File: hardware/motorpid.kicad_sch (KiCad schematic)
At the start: 108 parts, among them J1 BNC, J2 BNC, J3 BNC, J4 MOTOR + - shield, J5 POT 1 (+) 2 (wiper) 3 (-), J6 +15 / GND / -15, M1 fader motor, Q1 MJD44H11, Q2 MJD45H11, SW1 TARGET SOURCE, SW2 LOOP, SW3 D IN / OFF, SW4 I IN / OFF, SW5 D CAPACITOR, U1 LM321, U2 LM321, U3 LM321, U4 LM321, U5 LM321, U6 LM321, U7 LM321

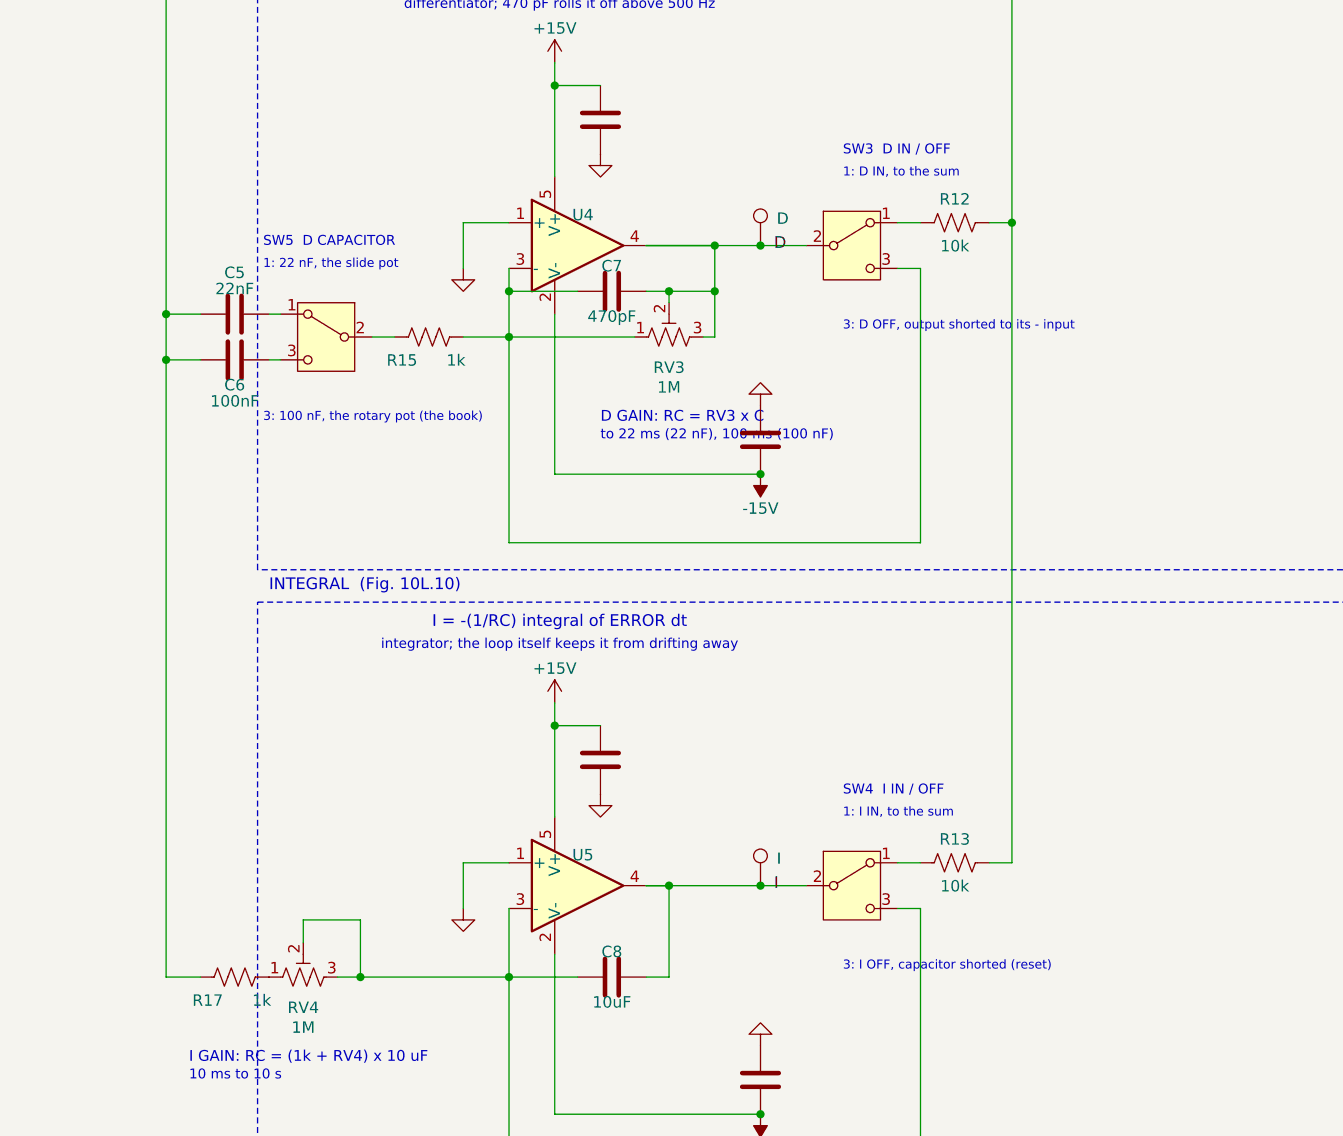
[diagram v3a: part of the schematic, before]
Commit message: D/I switches: pole 3 into the sum, pole 1 shorts; D capacitor switch ahead of its capacitors (common on the ERROR side), so each slide switch's three wires leave its one-sided pins without crossing
Co-Authored-By: Claude Fable 5.1 <noreply@anthropic.com>
Claude-Session: https://claude.ai/code/session_017Q2PYKR2UewvTfQgKmRJsG
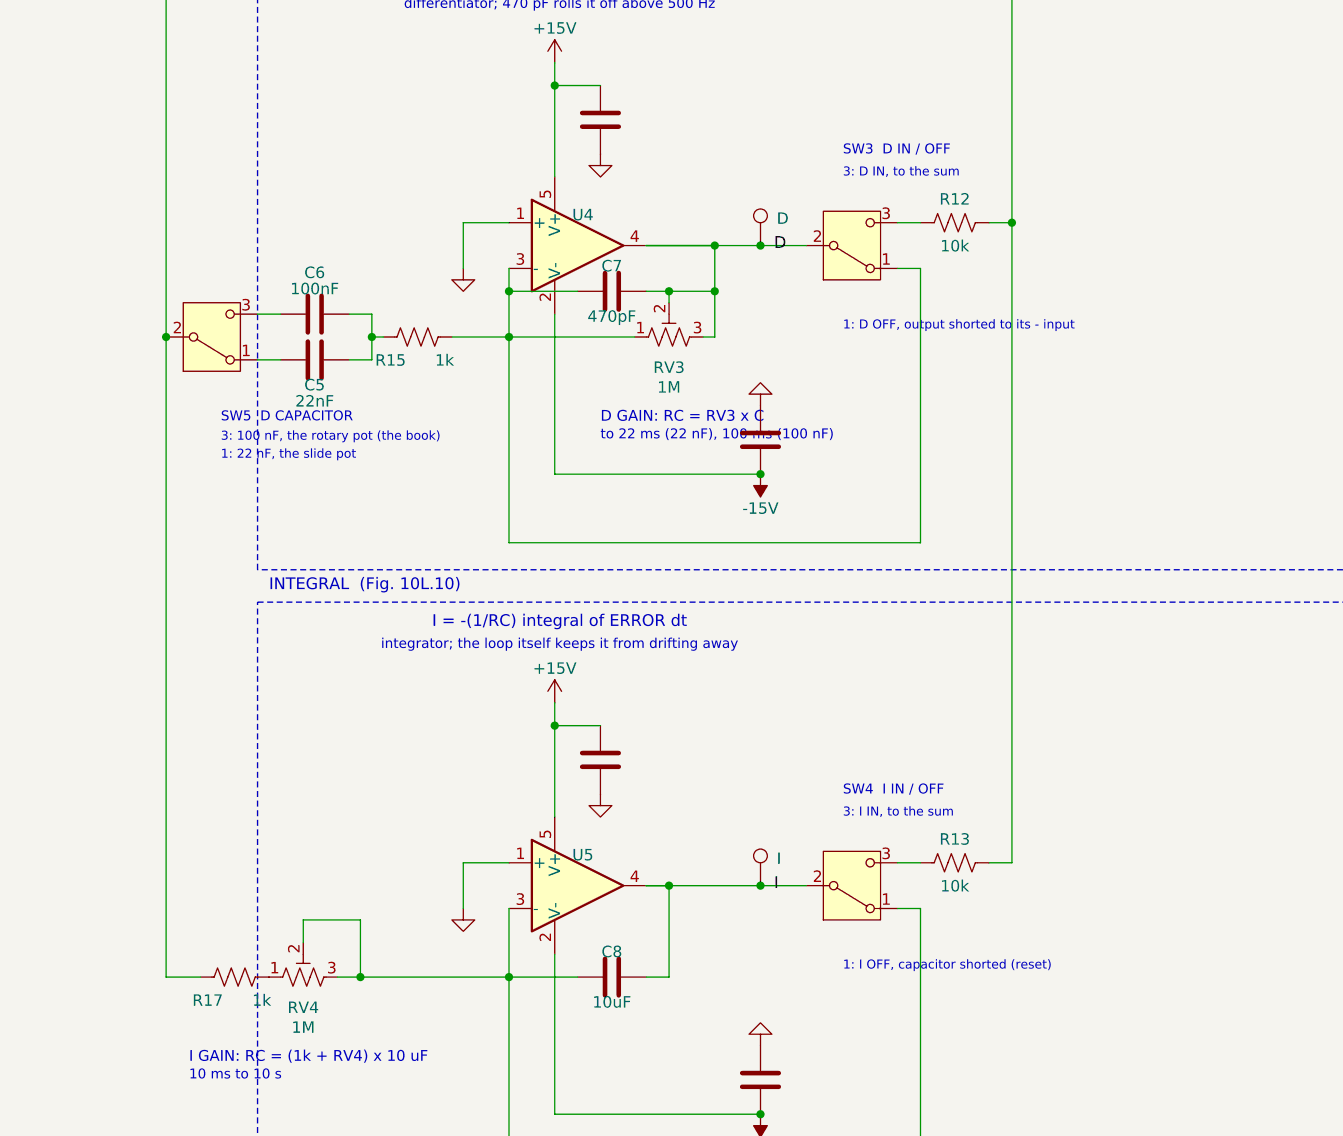
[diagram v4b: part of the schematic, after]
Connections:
- net ERROR: now also SW5.2 (B); no longer C5.1, C6.1
- net at C7.1, R15.2, RV3.1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: now also SW3.1 (A); no longer SW3.3 (C)
- net at R12.1: now also SW3.3 (C); no longer SW3.1 (A)
- net at C8.1, RV4.2, RV4.3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: now also SW4.1 (A); no longer SW4.3 (C)
- net at SW5.1 (A): now also C5.1; no longer C5.2
- net at R13.1: now also SW4.3 (C); no longer SW4.1 (A)
- net at C6.2: now also C5.2, R15.1; no longer SW5.3 (C)
- new net: C6.1, SW5.3 (C)
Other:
- note added: "1: D OFF, output shorted to its - input"
- note added: "1: I OFF, capacitor shorted (reset)"
- note added: "3: D IN, to the sum"
- note added: "3: I IN, to the sum"
- note removed: "1: D IN, to the sum"
- note removed: "1: I IN, to the sum"
- note removed: "3: D OFF, output shorted to its - input"
- note removed: "3: I OFF, capacitor shorted (reset)"
- moved on the sheet: C5, C6, R15

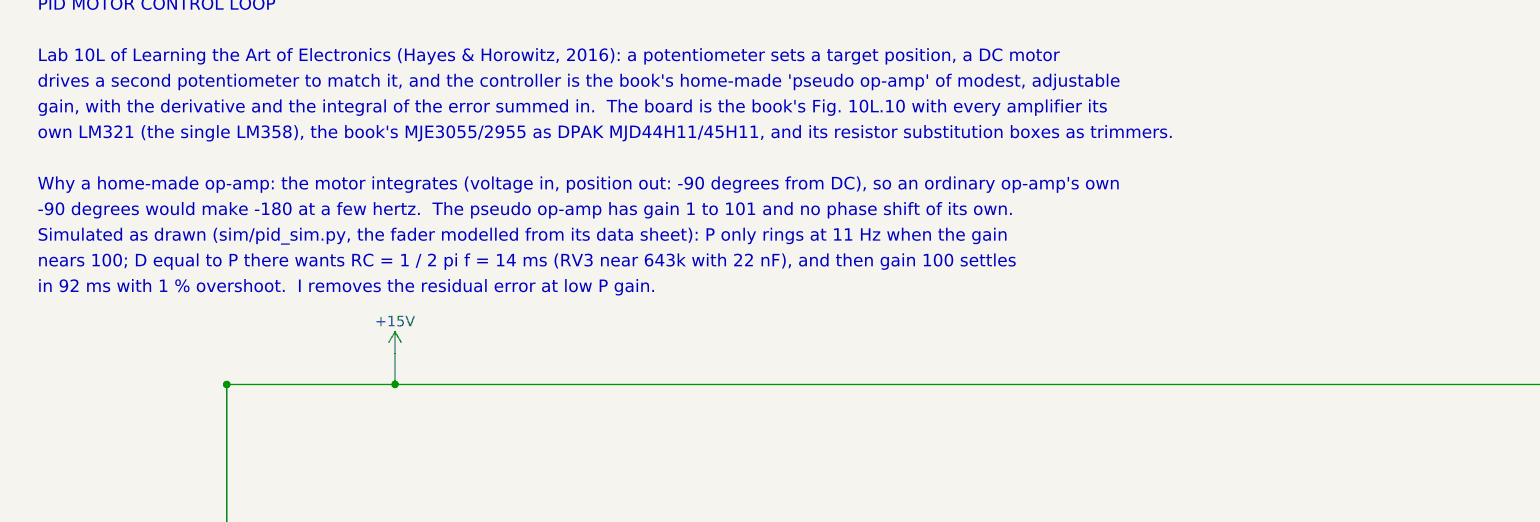
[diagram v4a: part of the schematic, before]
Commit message: Fab package, documents, simulation update and chat log for rev A: build passes end to end (ERC 0, 243 circuit checks, DRC 0, fab checks, 23 document claims)
Co-Authored-By: Claude Fable 5.1 <noreply@anthropic.com>
Claude-Session: https://claude.ai/code/session_017Q2PYKR2UewvTfQgKmRJsG
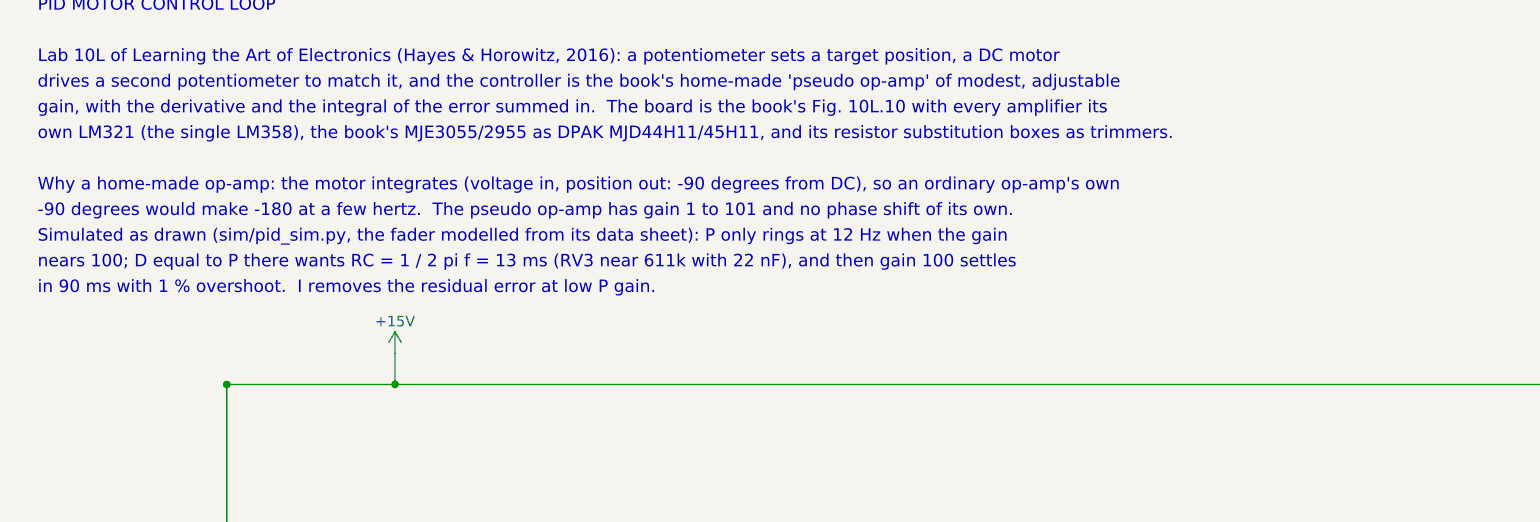
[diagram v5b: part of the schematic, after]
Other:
- note added: "Simulated as drawn (sim/pid_sim.py, the fader modelled from its data sheet): P only rings at 12 Hz when the gain"
- note added: "in 90 ms with 1 % overshoot. I removes the residual error at low P gain."
- note added: "nears 100; D equal to P there wants RC = 1 / 2 pi f = 13 ms (RV3 near 611k with 22 nF), and then gain 100 settles"
- note removed: "Simulated as drawn (sim/pid_sim.py, the fader modelled from its data sheet): P only rings at 11 Hz when the gain"
- note removed: "in 92 ms with 1 % overshoot. I removes the residual error at low P gain."
- note removed: "nears 100; D equal to P there wants RC = 1 / 2 pi f = 14 ms (RV3 near 643k with 22 nF), and then gain 100 settles"
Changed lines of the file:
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@@
+	)
+	(rectangle
+		(start 454.2 119.08)
+		(end 513.3 193.1)
+		(stroke
+			(width 0.15)
+			(type dash)
+		)
+		(fill
+			(type none)
+		)
+	)
+	(rectangle
+		(start 193.04 166.62)
+		(end 320.04 234.14)
+		(stroke
+			(width 0.15)
+			(type dash)
+		)
+		(fill
+			(type none)
+		)
+	)
+	(rectangle
+		(start 410.02 96.58)
+		(end 452.85 162.08)
+		(stroke
+			(width 0.15)
+			(type dash)
+		)
+		(fill
+			(type none)
+		)
 	)
 	(rectangle
@@
 	)
 	(rectangle
-		(start 454.2 119.08)
-		(end 513.3 193.1)
-		(stroke
-			(width 0.15)
-			(type dash)
-		)
-		(fill
-			(type none)
-		)
-	)
-	(rectangle
-		(start 193.04 166.62)
-		(end 320.04 234.14)
-		(stroke
-			(width 0.15)
-			(type dash)
-		)
-		(fill
-			(type none)
-		)
-	)
-	(rectangle
 		(start 124.46 100.08)
 		(end 320.04 164.08)
@@
 		)
 	)
-	(rectangle
-		(start 410.02 96.58)
-		(end 452.85 162.08)
-		(stroke
-			(width 0.15)
-			(type dash)
-		)
-		(fill
-			(type none)
-		)
-	)
 	(text "6.8k ends keep it to ±6.4 V, inside what the motor pot"
 		(exclude_from_sim no)
@@
 		)
 	)
+	(text "in 90 ms with 1 % overshoot.  I removes the residual error at low P gain."
+		(exclude_from_sim no)
+		(at 33.02 54.42 0)
+		(effects
+			(font
+				(size 1.5 1.5)
+			)
+			(justify left)
+		)
+	)
 	(text "TARGET"
 		(exclude_from_sim no)
@@
 		)
 	)
-	(text "Simulated as drawn (sim/pid_sim.py, the fader modelled from its data sheet): P only rings at 11 Hz when the gain"
+	(text "Simulated as drawn (sim/pid_sim.py, the fader modelled from its data sheet): P only rings at 12 Hz when the gain"
 		(exclude_from_sim no)
 		(at 33.02 48.22 0)
@@
 		)
 	)
-	(text "nears 100; D equal to P there wants RC = 1 / 2 pi f = 14 ms (RV3 near 643k with 22 nF), and then gain 100 settles"
+	(text "nears 100; D equal to P there wants RC = 1 / 2 pi f = 13 ms (RV3 near 611k with 22 nF), and then gain 100 settles"
 		(exclude_from_sim no)
 		(at 33.02 51.32 0)
@@
 			)
 			(justify left)
-		)
-	)
-	(text "in 92 ms with 1 % overshoot.  I removes the residual error at low P gain."
-		(exclude_from_sim no)
-		(at 33.02 54.42 0)
-		(effects
-			(font
-				(size 1.5 1.5)
-			)
-			(justify left)

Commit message: Clockwise arcs over the knob and the three trimmers (Bourns CW = terminal 3; rheostats 1-2, wiper ties under the bodies); handbook's I GAIN direction fixed; Jason's answers recorded: fuse kept, size kept, MSK12C02 travel from its section, fader measurements to make
Co-Authored-By: Claude Fable 5.1 <noreply@anthropic.com>
Claude-Session: https://claude.ai/code/session_017Q2PYKR2UewvTfQgKmRJsG
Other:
- note added: "Trimmers: clockwise is more resistance (Bourns: wiper"
- note added: "clockwise: more R, LESS I"
- note added: "clockwise: more R, more D"
- note added: "clockwise: more R, more P"
- note added: "to 3), so more P, more D, but LESS I. Arcs on the board."
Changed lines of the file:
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@@
+	)
+	(rectangle
+		(start 410.02 96.58)
+		(end 452.85 162.08)
+		(stroke
+			(width 0.15)
+			(type dash)
+		)
+		(fill
+			(type none)
+		)
+	)
+	(rectangle
+		(start 124.46 100.08)
+		(end 320.04 164.08)
+		(stroke
+			(width 0.15)
+			(type dash)
+		)
+		(fill
+			(type none)
+		)
+	)
+	(rectangle
+		(start 193.04 166.62)
+		(end 320.04 234.14)
+		(stroke
+			(width 0.15)
+			(type dash)
+		)
+		(fill
+			(type none)
+		)
+	)
+	(rectangle
+		(start 193.04 237.74)
+		(end 320.04 305.26)
+		(stroke
+			(width 0.15)
+			(type dash)
+		)
+		(fill
+			(type none)
+		)
 	)
 	(rectangle
@@
 		)
 	)
-	(rectangle
-		(start 193.04 166.62)
-		(end 320.04 234.14)
-		(stroke
-			(width 0.15)
-			(type dash)
-		)
-		(fill
-			(type none)
-		)
-	)
-	(rectangle
-		(start 410.02 96.58)
-		(end 452.85 162.08)
-		(stroke
-			(width 0.15)
-			(type dash)
-		)
-		(fill
-			(type none)
-		)
-	)
-	(rectangle
-		(start 193.04 237.74)
-		(end 320.04 305.26)
-		(stroke
-			(width 0.15)
-			(type dash)
-		)
-		(fill
-			(type none)
-		)
-	)
-	(rectangle
-		(start 124.46 100.08)
-		(end 320.04 164.08)
-		(stroke
-			(width 0.15)
-			(type dash)
-		)
-		(fill
-			(type none)
-		)
-	)
 	(text "6.8k ends keep it to ±6.4 V, inside what the motor pot"
 		(exclude_from_sim no)
@@
 		)
 	)
+	(text "to 3), so more P, more D, but LESS I.  Arcs on the board."
+		(exclude_from_sim no)
+		(at 238.76 373.315 0)
+		(effects
+			(font
+				(size 1.3 1.3)
+			)
+			(justify left)
+		)
+	)
 	(text "stops.  The loop runs the motor at 50-150 mA rms."
 		(exclude_from_sim no)
@@
 		)
 	)
+	(text "clockwise: more R, more P"
+		(exclude_from_sim no)
+		(at 287.02 155.24 0)
+		(effects
+			(font
+				(size 1.1 1.1)
+			)
+			(justify left)
+		)
+	)
 	(text "the motorized slide pot (external, on flying"
 		(exclude_from_sim no)
@@
 		)
 	)
+	(text "clockwise: more R, more D"
+		(exclude_from_sim no)
+		(at 231.14 221.28 0)
+		(effects
+			(font
+				(size 1.1 1.1)
+			)
+			(justify left)
+		)
+	)
 	(text "POWER"
 		(exclude_from_sim no)
@@
 		)
 	)
+	(text "clockwise: more R, LESS I"
+		(exclude_from_sim no)
+		(at 185.42 292.4 0)
+		(effects
+			(font
+				(size 1.1 1.1)
+			)
+			(justify left)
+		)
+	)
 	(text "Op-amps are drawn + on top: that is how the SOT-23-5 sits."
 		(exclude_from_sim no)
@@
 			)
 			(justify left)
+		)
+	)
+	(text "Trimmers: clockwise is more resistance (Bourns: wiper"
+		(exclude_from_sim no)
+		(at 238.76 370.78 0)
+		(effects
+			(font
+				(size 1.3 1.3)
+			)
+			(justify left)

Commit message: Probe loops on BASES, U6 OUT and U7 OUT; LOOP explained on the schematic, front, back and handbook (open = DRIVE from TARGET); ground moved clear of RV4's I; back silkscreen rewritten one item per line with https URL
Co-Authored-By: Claude Opus 5.5 <noreply@anthropic.com>
Claude-Session: https://claude.ai/code/session_017Q2PYKR2UewvTfQgKmRJsG
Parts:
- added TP12: BASES, motorpid:TestPoint_Loop_RH-5019, symbol Connector:TestPoint
- added TP13: U6 OUT, motorpid:TestPoint_Loop_RH-5019, symbol Connector:TestPoint
- added TP14: U7 OUT, motorpid:TestPoint_Loop_RH-5019, symbol Connector:TestPoint
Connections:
- net BASES: now also TP12.1
- net at R25.1, U7.3 (-), U7.4: now also TP14.1
- net at C9.2, R19.1, U6.4: now also TP13.1
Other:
- note added: "(x1 with P GAIN anticlockwise, D and I off)"
- note added: "1 = OPEN: no feedback. U1's - side gets ground,"
- note added: "3 = CLOSED: POSITION fed back, the PID loop"
- note added: "CLOSED (3): POSITION, the fader's wiper: the loop."
- note added: "LOOP (SW2): which voltage U1 subtracts from TARGET."
- note added: "OPEN (1): ground, so ERROR = TARGET and the motor"
- note added: "anticlockwise, D and I off). The slider runs to an end."
- note added: "driver gets P GAIN x TARGET, open loop: the knob or a"
- note added: "generator drives the motor directly (x1 with P GAIN"
- note added: "so ERROR = TARGET: DRIVE = P GAIN x TARGET"
- note removed: "CLOSED: the pot's voltage into the difference amplifier."
- note removed: "LOOP (SW2)"
- note removed: "OPEN: its - input grounded, so the motor runs to an end"
- note removed: "lower pole 3: CLOSED (position)"
- note removed: "stop as the knob leaves zero (the book's first test)."
- note removed: "upper pole 1: OPEN (- input grounded)"

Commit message: Fader measured and identified: Bourns PSM01-082A-103B2 (taper B2, A+ toward 1), plant refit to Jason's bench numbers (14 ohm, 2-3 V breakaway, 0.16 A running); stick-slip triangle sim; D rule now 234k; 1M trimmers kept; low-drive stall heats the driver (open, warnings added)
Co-Authored-By: Claude Opus 5.5 <noreply@anthropic.com>
Claude-Session: https://claude.ai/code/session_017Q2PYKR2UewvTfQgKmRJsG
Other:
- note added: "10k track and a 6-11 V motor. Bourns: motor A to MOTOR,"
- note added: "20 it overshoots; near 100 (P only) it rings: the period"
- note added: "234k with the 22 nF; for the book's rotary motor-pot"
- note added: "A ±3 V square wave at 0.2 Hz on the jack gives steps;"
- note added: "At P gain 1.5 a 1 V step cannot unstick the slider; near"
- note added: "B to GND; track 1, 2, 3 to POT 1, 2, 3 (A + moves the"
- note added: "FUSE: not in the book. The 0.35 A PTC opens a full-drive"
- note added: "Simulated as drawn (sim/pid_sim.py, the fader modelled from bench measurements): P only rings at 31 Hz when the gain"
- note added: "The lab's Bourns PSM01-082A-103B2, or any fader with a"
- note added: "The servo track (1' 2' 3') and touch pin T stay free."
- note added: "a transistor takes up to 3.7 W. 1 ohm per emitter reads"
- note added: "a ±3 V triangle at 0.05 Hz, stick-slip. ±12 V max."
- note added: "and stalls there: bring TARGET back to 0 within seconds."
- note added: "anticlockwise, D and I off). The slider runs to an end"
- note added: "in 28 ms with 3 % overshoot. I removes the residual error at low P gain."
- note added: "leads): Bourns PSM01-082A-103B2 or any fader"
- note added: "lever toward 1). Others: POT 1 to the end that must"
- note added: "nears 100; D equal to P there wants RC = 1 / 2 pi f = 5 ms (RV3 near 234k with 22 nF), and then gain 100 settles"
- note added: "read +7.7 V; if the loop runs away, swap the motor wires."
- note added: "stall (0.6 A) in seconds and a short in well under one,"
- note added: "then resets itself. A stall at a few volts it holds, and"
- note added: "this slide pot (T about 32 ms) that is 5 ms, about"
- note added: "with a 10k track and a 6-11 V motor"
- note removed: "(0.6 A) in seconds and a short in well under one, then"
- note removed: "640k with the 22 nF; for the book's rotary motor-pot"
- note removed: "A ±0.5 V square wave at 0.2 Hz from a generator on the"
- note removed: "Any motorized fader with a 10k track and a 6-11 V motor."
- note removed: "At P gain 1.5 the loop is stable and slow; near 20 it"
- note removed: "FUSE: not in the book. The 0.35 A PTC opens a stall"
- note removed: "Simulated as drawn (sim/pid_sim.py, the fader modelled from its data sheet): P only rings at 12 Hz when the gain"
- note removed: "Watch the fuse lamp: a stall trips it."
- note removed: "Wire POT 1 to the track end that must read +7.7 V, 3 to"
- note removed: "a 10k track and a 6-11 V motor"
- note removed: "anticlockwise, D and I off). The slider runs to an end."
- note removed: "in 90 ms with 1 % overshoot. I removes the residual error at low P gain."
- note removed: "jack gives repeatable steps. TARGET IN ±12 V max."
- note removed: "leads): SparkFun COM-10976 or any fader with"
- note removed: "loop runs away, swap the two motor wires. The second"
- note removed: "nears 100; D equal to P there wants RC = 1 / 2 pi f = 13 ms (RV3 near 611k with 22 nF), and then gain 100 settles"
- note removed: "overshoots; near 100 (P only) it oscillates: the period"
- note removed: "positive drive moves the wiper toward POT 1. If the"
- note removed: "resets itself when it cools. 1 ohm per emitter reads"
- note removed: "the other, 2 to the wiper; MOTOR + and - so that a"
- note removed: "the slide pot (T of 40-90 ms) that is 6-14 ms, 300k-"
- note removed: "track and the touch pin of the SparkFun fader stay unused."
